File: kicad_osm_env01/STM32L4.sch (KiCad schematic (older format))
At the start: 10 parts

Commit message: kicad review sch initial
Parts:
- added D?: STM_STATUS, symbol device:LED
- added R?: 330R, Resistor_SMD:R_0603_1608Metric, symbol OSM_env01-rescue:R-device-ESP32-EVB_Rev_D-rescue
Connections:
- net GND: now also D?.1 (K)
- net PA15: no longer names the net of U?.25 (PA15)
- net PA15: now also R?.1
- new net: D?.2 (A), R?.2
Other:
- note added: "check led polarity\n"
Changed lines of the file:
@@
 $Descr A4 11693 8268
 encoding utf-8
-Sheet 8 9
+Sheet 5 9
 Title ""
 Date ""
@@
 Wire Wire Line
 	8675 3325 8575 3325
-Text HLabel 8675 3425 2    50   Input ~ 0
-PA15
-Wire Wire Line
-	8675 3425 8575 3425
 Text HLabel 8675 3525 2    50   Input ~ 0
 PA14
@@
 Wire Wire Line
 	8675 3625 8575 3625
+Wire Wire Line
+	10100 3425 10400 3425
+$Comp
+L OSM_env01-rescue:GND-ESP32-EVB_Rev_D #PWR?
+U 1 1 60BF8FB6
+P 10400 3425
+AR Path="/60BF8FB6" Ref="#PWR?"  Part="1"
+AR Path="/60917DD5/60BF8FB6" Ref="#PWR?"  Part="1"
+F 0 "#PWR?" H 10400 3175 50  0001 C CNN
+F 1 "GND" H 10405 3252 50  0000 C CNN
+F 2 "" H 10400 3425 60  0000 C CNN
+F 3 "" H 10400 3425 60  0000 C CNN
+	1    10400 3425
+	1    0    0    -1
+$EndComp
+Wire Wire Line
+	9800 3425 9650 3425
+$Comp
+L OSM_env01-rescue:R-device-ESP32-EVB_Rev_D-rescue R?
+U 1 1 60BF8FBD
+P 9500 3425
+AR Path="/60BF8FBD" Ref="R?"  Part="1"
+AR Path="/60917DD5/60BF8FBD" Ref="R?"  Part="1"
+F 0 "R?" V 9293 3425 50  0000 C CNN
+F 1 "330R" V 9384 3425 50  0000 C CNN
+F 2 "Resistor_SMD:R_0603_1608Metric" V 9430 3425 50  0001 C CNN
+F 3 "" H 9500 3425 50  0001 C CNN
+	1    9500 3425
+	0    -1   -1   0
+$EndComp
+Wire Wire Line
+	8575 3425 9350 3425
+$Comp
+L device:LED D?
+U 1 1 60C00D45
+P 9950 3425
+F 0 "D?" H 9943 3170 50  0000 C CNN
+F 1 "STM_STATUS" H 9943 3261 50  0000 C CNN
+F 2 "" H 9950 3425 50  0001 C CNN
+F 3 "~" H 9950 3425 50  0001 C CNN
+	1    9950 3425
+	-1   0    0    1
+$EndComp
+Text Notes 10100 3925 0    50   ~ 0
+check led polarity\n
 $EndSCHEMATC

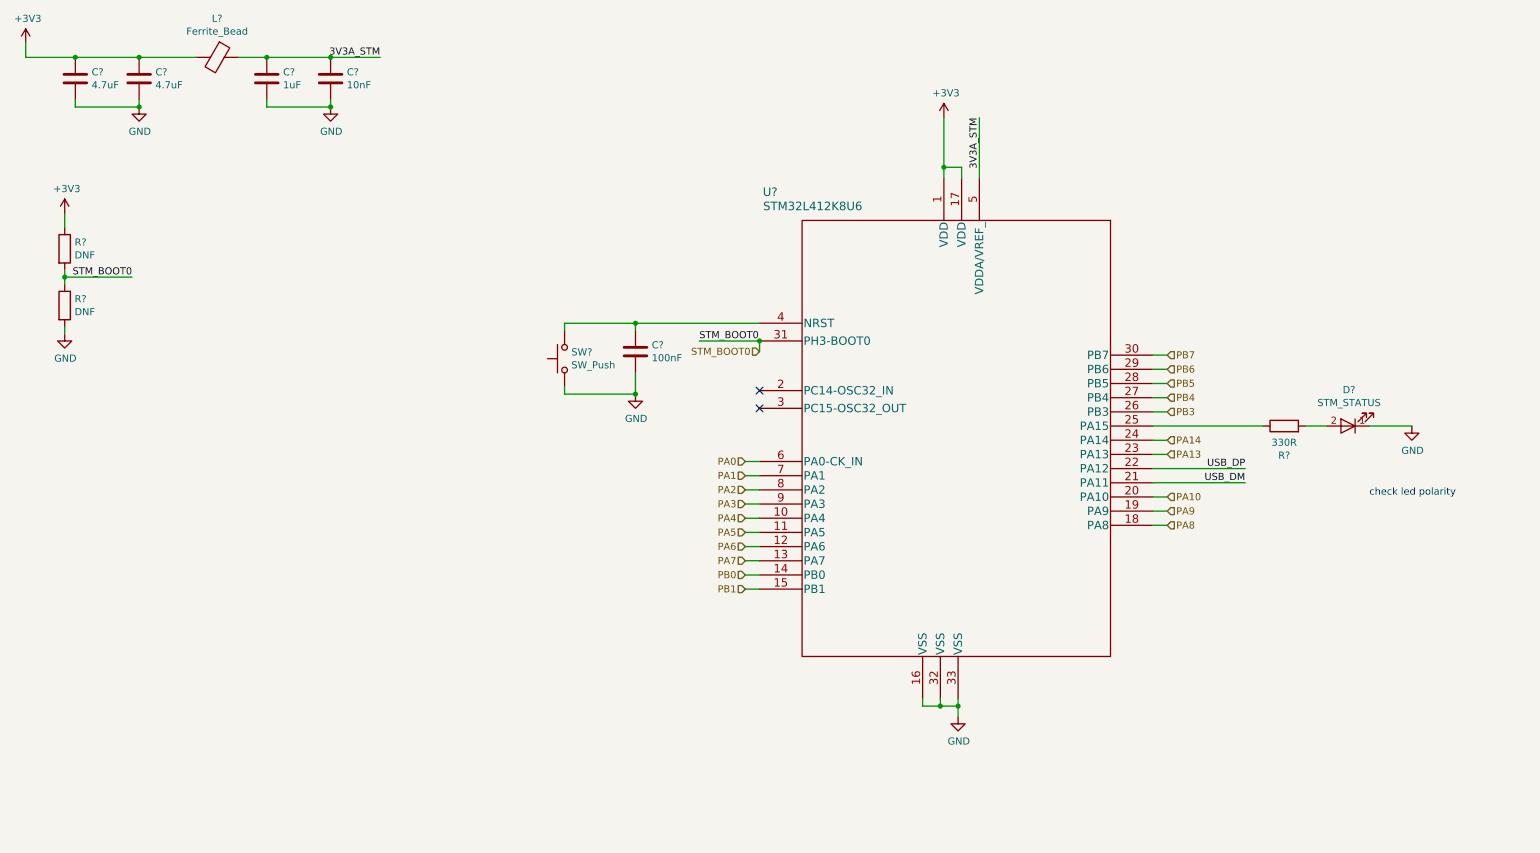
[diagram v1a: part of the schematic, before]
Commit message: updated schematics
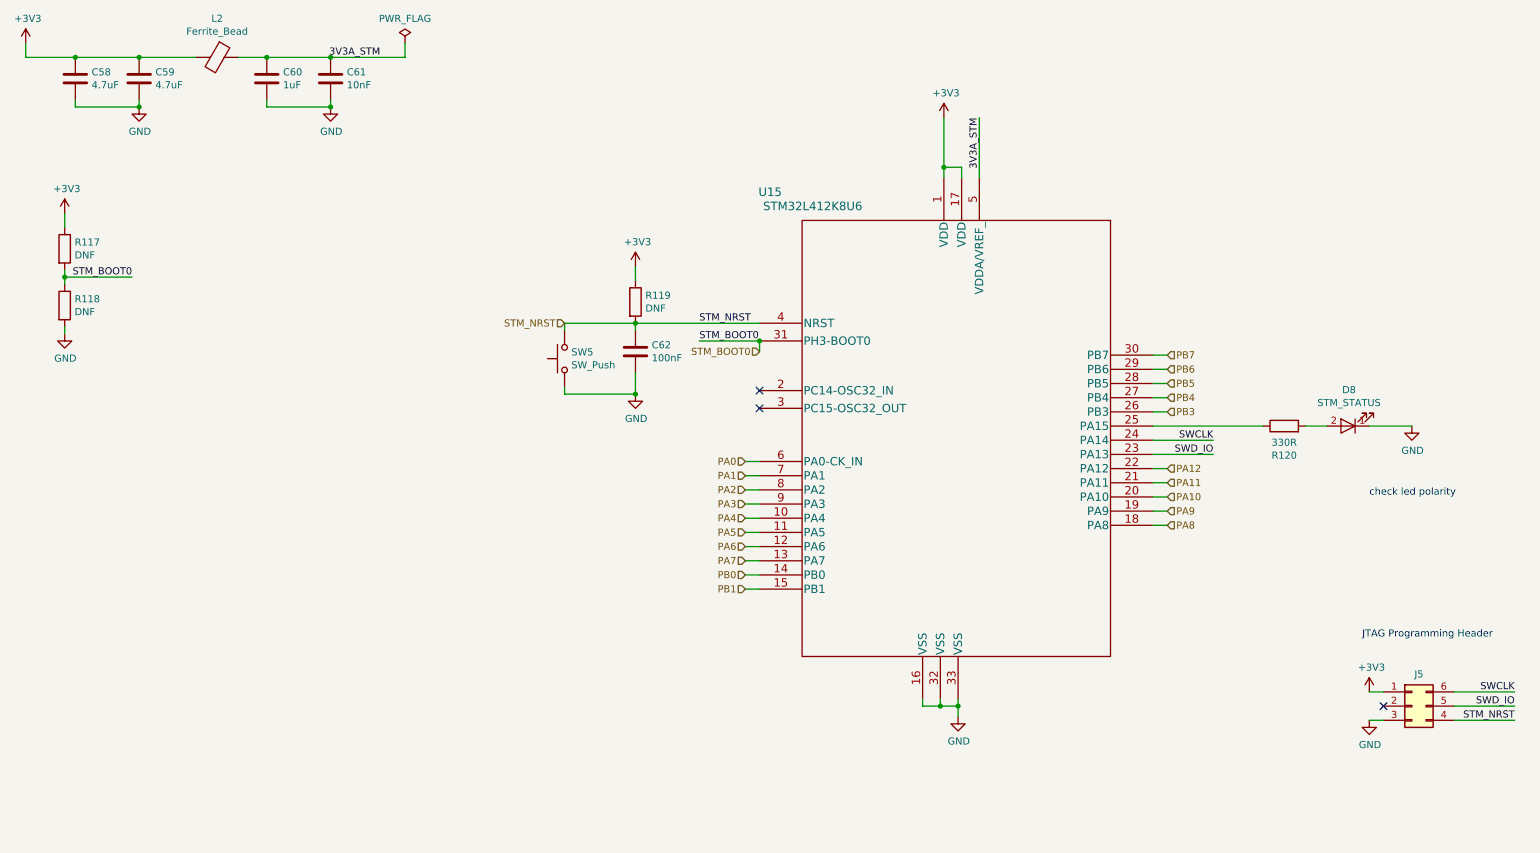
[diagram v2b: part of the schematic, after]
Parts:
- added J5: Conn_02x03_Counter_Clockwise, symbol Connector:Conn_02x03_Counter_Clockwise
- added R119: DNF, symbol device:R
- gave numbers to parts that had none: 12
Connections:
- net +3V3: now also J5.1 (Pin_1), R119.1
- net GND: now also J5.3 (Pin_3)
- net STM_NRST: now reaches C62.1, SW5.2, U15.4 (NRST)
- net STM_NRST: now also J5.4 (Pin_4), R119.2
- net PA13 renamed SWD_IO
- net SWD_IO: now also J5.5 (Pin_5)
- net PA14 renamed SWCLK
- net SWCLK: now also J5.6 (Pin_6)
- net USB_DM renamed PA11
- net USB_DP renamed PA12
- no-connect marks 2 -> 3
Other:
- note added: "JTAG Programming Header"

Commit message: schematics awaiting review
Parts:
- added TP85: Test_Point, TestPoint:TestPoint_THTPad_D1.0mm_Drill0.5mm, symbol OSM_env01-rescue:Test_Point-Connector-ESP32-EVB_Rev_D-rescue
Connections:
- net 3V3A_STM: now also TP85.1
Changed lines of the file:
@@
 Wire Wire Line
 	2775 825  3300 825
+$Comp
+L OSM_env01-rescue:Test_Point-Connector-ESP32-EVB_Rev_D-rescue TP?
+U 1 1 60C1B460
+P 3300 825
+AR Path="/60C1B460" Ref="TP?"  Part="1"
+AR Path="/608F4675/60C1B460" Ref="TP?"  Part="1"
+AR Path="/60917DD5/60C1B460" Ref="TP85"  Part="1"
+F 0 "TP85" V 3300 1075 50  0000 C CNN
+F 1 "Test_Point" V 3300 1200 50  0001 C CNN
+F 2 "TestPoint:TestPoint_THTPad_D1.0mm_Drill0.5mm" H 3500 825 50  0001 C CNN
+F 3 "~" H 3500 825 50  0001 C CNN
+	1    3300 825
+	0    1    -1   0
+$EndComp
 $EndSCHEMATC

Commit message: updated schematics
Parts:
- C58, C59, C60, C61, C62: footprint (none) -> Capacitor_SMD:C_0603_1608Metric
- D8: footprint (none) -> LED_SMD:LED_0603_1608Metric
- J5: footprint (none) -> Connector_PinHeader_2.54mm:PinHeader_2x03_P2.54mm_Vertical
- L2: footprint (none) -> Inductor_SMD:L_0805_2012Metric
- R117, R118, R119: footprint (none) -> Resistor_SMD:R_0603_1608Metric
- SW5: footprint (none) -> Button_Switch_SMD:SW_SPST_B3U-1000P
- U15: footprint QFN32_5X5_STM -> Package_DFN_QFN:QFN-32-1EP_5x5mm_P0.5mm_EP3.1x3.1mm
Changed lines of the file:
@@
 $Descr A4 11693 8268
 encoding utf-8
-Sheet 10 11
+Sheet 10 12
 Title ""
 Date ""
@@
 F 0 "C58" H 1090 1021 50  0000 L CNN
 F 1 "4.7uF" H 1090 930 50  0000 L CNN
-F 2 "" H 1013 825 50  0001 C CNN
+F 2 "Capacitor_SMD:C_0603_1608Metric" H 1013 825 50  0001 C CNN
 F 3 "" H 975 975 50  0001 C CNN
 	1    975  975
@@
 F 0 "C59" H 1540 1021 50  0000 L CNN
 F 1 "4.7uF" H 1540 930 50  0000 L CNN
-F 2 "" H 1463 825 50  0001 C CNN
+F 2 "Capacitor_SMD:C_0603_1608Metric" H 1463 825 50  0001 C CNN
 F 3 "" H 1425 975 50  0001 C CNN
 	1    1425 975
@@
 F 0 "C60" H 2440 1021 50  0000 L CNN
 F 1 "1uF" H 2440 930 50  0000 L CNN
-F 2 "" H 2363 825 50  0001 C CNN
+F 2 "Capacitor_SMD:C_0603_1608Metric" H 2363 825 50  0001 C CNN
 F 3 "" H 2325 975 50  0001 C CNN
 	1    2325 975
@@
 F 0 "C61" H 2890 1021 50  0000 L CNN
 F 1 "10nF" H 2890 930 50  0000 L CNN
-F 2 "" H 2813 825 50  0001 C CNN
+F 2 "Capacitor_SMD:C_0603_1608Metric" H 2813 825 50  0001 C CNN
 F 3 "" H 2775 975 50  0001 C CNN
 	1    2775 975
@@
 F 0 "L2" V 1701 825 50  0000 C CNN
 F 1 "Ferrite_Bead" V 1792 825 50  0000 C CNN
-F 2 "" V 1905 825 50  0001 C CNN
+F 2 "Inductor_SMD:L_0805_2012Metric" V 1905 825 50  0001 C CNN
 F 3 "" H 1975 825 50  0001 C CNN
 	1    1975 825
@@
 F 0 "U15" H 5875 2575 60  0000 C CNN
 F 1 "STM32L412K8U6" H 6175 2475 60  0000 C CNN
-F 2 "QFN32_5X5_STM" H 7200 2415 60  0001 C CNN
+F 2 "Package_DFN_QFN:QFN-32-1EP_5x5mm_P0.5mm_EP3.1x3.1mm" H 7200 2415 60  0001 C CNN
 F 3 "" H 5800 2175 60  0000 C CNN
 	1    5800 2175
@@
 F 0 "R118" H 970 2621 50  0000 L CNN
 F 1 "DNF" H 970 2530 50  0000 L CNN
-F 2 "" V 830 2575 50  0001 C CNN
+F 2 "Resistor_SMD:R_0603_1608Metric" V 830 2575 50  0001 C CNN
 F 3 "" H 900 2575 50  0001 C CNN
 	1    900  2575
@@
 F 0 "R117" H 970 2221 50  0000 L CNN
 F 1 "DNF" H 970 2130 50  0000 L CNN
-F 2 "" V 830 2175 50  0001 C CNN
+F 2 "Resistor_SMD:R_0603_1608Metric" V 830 2175 50  0001 C CNN
 F 3 "" H 900 2175 50  0001 C CNN
 	1    900  2175
@@
 F 0 "C62" H 5040 2946 50  0000 L CNN
 F 1 "100nF" H 5040 2855 50  0000 L CNN
-F 2 "" H 4963 2750 50  0001 C CNN
+F 2 "Capacitor_SMD:C_0603_1608Metric" H 4963 2750 50  0001 C CNN
 F 3 "" H 4925 2900 50  0001 C CNN
 	1    4925 2900
@@
 F 0 "SW5" V 4471 2902 50  0000 R CNN
 F 1 "SW_Push" V 4380 2902 50  0000 R CNN
-F 2 "" H 4425 3150 50  0001 C CNN
+F 2 "Button_Switch_SMD:SW_SPST_B3U-1000P" H 4425 3150 50  0001 C CNN
 F 3 "" H 4425 3150 50  0001 C CNN
 	1    4425 2950
@@
 F 0 "D8" H 9943 3170 50  0000 C CNN
 F 1 "STM_STATUS" H 9943 3261 50  0000 C CNN
-F 2 "" H 9950 3425 50  0001 C CNN
+F 2 "LED_SMD:LED_0603_1608Metric" H 9950 3425 50  0001 C CNN
 F 3 "~" H 9950 3425 50  0001 C CNN
 	1    9950 3425
@@
 F 0 "R119" H 4995 2596 50  0000 L CNN
 F 1 "DNF" H 4995 2505 50  0000 L CNN
-F 2 "" V 4855 2550 50  0001 C CNN
+F 2 "Resistor_SMD:R_0603_1608Metric" V 4855 2550 50  0001 C CNN
 F 3 "" H 4925 2550 50  0001 C CNN
 	1    4925 2550
@@
 F 0 "J5" H 10450 5625 50  0000 C CNN
 F 1 "Conn_02x03_Counter_Clockwise" H 10450 5626 50  0001 C CNN
-F 2 "" H 10400 5400 50  0001 C CNN
+F 2 "Connector_PinHeader_2.54mm:PinHeader_2x03_P2.54mm_Vertical" H 10400 5400 50  0001 C CNN
 F 3 "~" H 10400 5400 50  0001 C CNN
 	1    10400 5400

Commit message: Throwdown of parts
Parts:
- removed R117, R118: DNF, Resistor_SMD:R_0603_1608Metric, symbol device:R
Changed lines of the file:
@@
 	5800 2825 5375 2825
-Wire Wire Line
-	900  2375 1375 2375
-Text Label 1375 2375 2    50   ~ 0
-STM_BOOT0
-Wire Wire Line
-	900  2375 900  2325
-Connection ~ 900  2375
-$Comp
-L power:+3V3 #PWR?
-U 1 1 60931F89
-P 900 1925
-AR Path="/60931F89" Ref="#PWR?"  Part="1"
-AR Path="/60917DD5/60931F89" Ref="#PWR0112"  Part="1"
-F 0 "#PWR0112" H 900 1775 50  0001 C CNN
-F 1 "+3V3" H 915 2098 50  0000 C CNN
-F 2 "" H 900 1925 50  0001 C CNN
-F 3 "" H 900 1925 50  0001 C CNN
-	1    900  1925
-	1    0    0    -1
-$EndComp
-Wire Wire Line
-	900  2025 900  1925
-Wire Wire Line
-	900  2775 900  2725
-$Comp
-L power:GND #PWR?
-U 1 1 60931F91
-P 900 2775
-AR Path="/60931F91" Ref="#PWR?"  Part="1"
-AR Path="/60917DD5/60931F91" Ref="#PWR0113"  Part="1"
-F 0 "#PWR0113" H 900 2525 50  0001 C CNN
-F 1 "GND" H 905 2602 50  0000 C CNN
-F 2 "" H 900 2775 50  0001 C CNN
-F 3 "" H 900 2775 50  0001 C CNN
-	1    900  2775
-	1    0    0    -1
-$EndComp
-Wire Wire Line
-	900  2425 900  2375
-$Comp
-L device:R R?
-U 1 1 60931F98
-P 900 2575
-AR Path="/60931F98" Ref="R?"  Part="1"
-AR Path="/60917DD5/60931F98" Ref="R118"  Part="1"
-F 0 "R118" H 970 2621 50  0000 L CNN
-F 1 "DNF" H 970 2530 50  0000 L CNN
-F 2 "Resistor_SMD:R_0603_1608Metric" V 830 2575 50  0001 C CNN
-F 3 "" H 900 2575 50  0001 C CNN
-	1    900  2575
-	1    0    0    -1
-$EndComp
-$Comp
-L device:R R?
-U 1 1 60931F9E
-P 900 2175
-AR Path="/60931F9E" Ref="R?"  Part="1"
-AR Path="/60917DD5/60931F9E" Ref="R117"  Part="1"
-F 0 "R117" H 970 2221 50  0000 L CNN
-F 1 "DNF" H 970 2130 50  0000 L CNN
-F 2 "Resistor_SMD:R_0603_1608Metric" V 830 2175 50  0001 C CNN
-F 3 "" H 900 2175 50  0001 C CNN
-	1    900  2175
-	1    0    0    -1
-$EndComp
 Wire Wire Line
 	4925 2700 5800 2700

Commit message: updated 3d step file
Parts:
- U15: symbol Devtank:STM32L412K8U6 -> OSM_env01-rescue:STM32L412K8U6-Devtank
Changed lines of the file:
@@
 STM_BOOT0
 $Comp
-L Devtank:STM32L412K8U6 U?
+L OSM_env01-rescue:STM32L412K8U6-Devtank U?
 U 1 1 60931F7E
 P 5800 2175

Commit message: added stm to schematic
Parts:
- removed D8: STM_STATUS, LED_SMD:LED_0603_1608Metric, symbol device:LED
- removed R120: 330R, Resistor_SMD:R_0603_1608Metric, symbol OSM_env01-rescue:R-device-ESP32-EVB_Rev_D-rescue
- removed U15: STM32L412K8U6, Package_DFN_QFN:QFN-32-1EP_5x5mm_P0.5mm_EP3.1x3.1mm, symbol OSM_env01-rescue:STM32L412K8U6-Devtank
- added C? (x2): 18pF, symbol device:C
- added C? (x2): 4.3pF, symbol device:C
- added D?: GRN, symbol device:LED
- added R? (x2): R, symbol device:R
- added R?: 330R, symbol device:R
- added U?: STM32L451RCTx, LQFP64, symbol Devtank:STM32L451RCTx
- added Y?: 8MHZ, symbol device:Crystal_GND24
- added Y?: ABS25-32.768KHZ-6-T, symbol device:Crystal_GND23
- L2: value Ferrite_Bead -> 2A/0.05DCR
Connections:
- net +3V3: now also D?.2 (A), R?.1, U?.19 (VDD), U?.32 (VDD), U?.48 (VDD), U?.64 (VDD)
- net 3V3A_STM: now also U?.13 (VDDA)
- net GND: now also C?.1, C?.1, C?.1, C?.1, R?.1, U?.12 (VSSA), U?.18 (VSS), U?.31 (VSS), U?.47 (VSS), U?.63 (VSS), Y?.2, Y?.2, Y?.3, Y?.4
- net STM_BOOT0: now also R?.2, R?.2, U?.60 (BOOT0)
- net STM_NRST: now also U?.7 (NRST)
- net SWCLK: now also U?.49 (SYS_JTCK-SWCLK/PA14)
- net SWD_IO: now also U?.46 (IR_OUT/SYS_JTMS-SWDIO/USB_OTG_FS_NOE/PA13)
- new net: D?.1 (K), R?.2
- new net 32.768KHZ_crystal_in: C?.2, U?.3 (PC14/RCC_OSC32_IN), Y?.1
- new net 32.768KHZ_crystal_out: C?.2, U?.4 (PC15/ADC1_EXTI15/ADC2_EXTI15/ADC3_EXTI15/RCC_OSC32_OUT), Y?.4
- new net 8MHZ_crystal_in: C?.2, U?.5 (PH0/RCC_OSC_IN), Y?.1
- new net 8MHZ_crystal_out: C?.2, U?.6 (PH1/RCC_OSC_OUT), Y?.3
- new net ADC1: U?.8 (PC0/ADC1_IN1/ADC2_IN1/ADC3_IN1/DFSDM_DATIN4/I2C3_SCL/LCD_SEG18/LPTIM1_IN1/LPTIM2_IN1/LPUART1_RX)
- new net ADC2: U?.9 (PC1/ADC1_IN2/ADC2_IN2/ADC3_IN2/DFSDM_CKIN4/I2C3_SDA/LCD_SEG19/LPTIM1_OUT/LPUART1_TX)
- new net ADC3: U?.10 (PC2/ADC1_IN3/ADC2_IN3/ADC3_IN3/DFSDM_CKOUT/LCD_SEG20/LPTIM1_IN2/SPI2_MISO)
- new net ADC4: U?.11 (PC3/ADC1_IN4/ADC2_IN4/ADC3_IN4/LCD_VLCD/LPTIM1_ETR/LPTIM2_ETR/SAI1_SD_A/SPI2_MOSI)
- new net ADC5: U?.14 (ADC1_IN5/ADC2_IN5/OPAMP1_VINP/RTC_TAMP2/SAI1_EXTCLK/SYS_WKUP1/TIM2_CH1/TIM2_ETR/TIM5_CH1/TIM8_ETR/UART4_TX/USART2_CTS/PA0)
- new net ADC6: U?.15 (ADC1_IN6/ADC2_IN6/LCD_SEG0/OPAMP1_VINM/TIM15_CH1N/TIM2_CH2/TIM5_CH2/UART4_RX/USART2_DE/USART2_RTS/PA1)
- new net CAN1_RX: U?.33 (DFSDM_DATIN1/I2C2_SMBA/LCD_SEG12/LPUART1_DE/LPUART1_RTS/SAI2_FS_A/SPI2_NSS/SWPMI1_IO/TIM15_BKIN/TIM1_BKIN/TIM1_BKIN_COMP2/TSC_G1_IO1/USART3_CK/PB12)
- new net CAN1_TX: U?.34 (DFSDM_CKIN1/I2C2_SCL/LCD_SEG13/LPUART1_CTS/SAI2_SCK_A/SPI2_SCK/SWPMI1_TX/TIM15_CH1N/TIM1_CH1N/TSC_G1_IO2/USART3_CTS/PB13)
- new net GPIO1: U?.37 (PC6/DFSDM_CKIN3/LCD_SEG24/SAI2_MCLK_A/SDMMC1_D6/TIM3_CH1/TIM8_CH1/TSC_G4_IO1)
- new net GPIO2: U?.38 (PC7/DFSDM_DATIN3/LCD_SEG25/SAI2_MCLK_B/SDMMC1_D7/TIM3_CH2/TIM8_CH2/TSC_G4_IO2)
- new net GPIO3: U?.39 (PC8/LCD_SEG26/SDMMC1_D0/TIM3_CH3/TIM8_CH3/TSC_G4_IO3)
- new net GPIO4: U?.40 (PC9/DAC1_EXTI9/LCD_SEG27/SAI2_EXTCLK/SDMMC1_D1/TIM3_CH4/TIM8_BKIN2/TIM8_BKIN2_COMP1/TIM8_CH4/TSC_G4_IO4/USB_OTG_FS_NOE)
- new net GPIO5: U?.51 (PC10/LCD_COM4/LCD_SEG28/LCD_SEG40/SAI2_SCK_B/SDMMC1_D2/SPI3_SCK/TSC_G3_IO2/UART4_TX/USART3_TX)
- new net GPIO6: U?.52 (PC11/ADC1_EXTI11/ADC2_EXTI11/ADC3_EXTI11/LCD_COM5/LCD_SEG29/LCD_SEG41/SAI2_MCLK_B/SDMMC1_D3/SPI3_MISO/TSC_G3_IO3/UART4_RX/USART3_RX)
- new net I2C1_SCL: U?.42 (DAC1_EXTI9/LCD_COM1/TIM15_BKIN/TIM1_CH2/USART1_TX/USB_OTG_FS_VBUS/PA9)
- new net I2C1_SDA: U?.43 (LCD_COM2/TIM17_BKIN/TIM1_CH3/USART1_RX/USB_OTG_FS_ID/PA10)
- new net LPUART1_RX: U?.29 (COMP1_OUT/DFSDM_DATIN7/I2C2_SCL/LCD_SEG10/LPUART1_RX/QUADSPI_CLK/SAI1_SCK_A/SPI2_SCK/TIM2_CH3/USART3_TX/PB10)
- new net LPUART1_TX: U?.30 (ADC1_EXTI11/ADC2_EXTI11/ADC3_EXTI11/COMP2_OUT/DFSDM_CKIN7/I2C2_SDA/LCD_SEG11/LPUART1_TX/QUADSPI_NCS/TIM2_CH4/USART3_RX/PB11)
- new net SPI1_CS: U?.20 (ADC1_IN9/ADC2_IN9/DAC1_OUT1/LPTIM2_OUT/SAI1_FS_B/SPI1_NSS/SPI3_NSS/USART2_CK/PA4)
- new net SPI1_MISO: U?.22 (ADC1_IN11/ADC2_IN11/LCD_SEG3/OPAMP2_VINP/QUADSPI_BK1_IO3/SPI1_MISO/TIM16_CH1/TIM1_BKIN/TIM1_BKIN_COMP2/TIM3_CH1/TIM8_BKIN/TIM8_BKIN_COMP2/USART3_CTS/PA6)
- new net SPI1_MOSI: U?.23 (ADC1_IN12/ADC2_IN12/LCD_SEG4/OPAMP2_VINM/QUADSPI_BK1_IO2/SPI1_MOSI/TIM17_CH1/TIM1_CH1N/TIM3_CH2/TIM8_CH1N/PA7)
- new net SPI1_SCK: U?.21 (ADC1_IN10/ADC2_IN10/DAC1_OUT2/LPTIM2_ETR/SPI1_SCK/TIM2_CH1/TIM2_ETR/TIM8_CH1N/PA5)
- new net USART1_RX: U?.59 (COMP2_INM/DFSDM_CKIN5/I2C1_SDA/LCD_SEG21/LPTIM1_IN2/SYS_PVD_IN/TIM17_CH1N/TIM4_CH2/TIM8_BKIN/TIM8_BKIN_COMP1/TSC_G2_IO4/UART4_CTS/USART1_RX/PB7)
- new net USART1_TX: U?.58 (COMP2_INP/DFSDM_DATIN5/I2C1_SCL/LPTIM1_ETR/SAI1_FS_B/TIM16_CH1N/TIM4_CH1/TIM8_BKIN2/TIM8_BKIN2_COMP2/TSC_G2_IO3/USART1_TX/PB6)
- new net USART2_RX: U?.17 (ADC1_IN8/ADC2_IN8/LCD_SEG2/OPAMP1_VOUT/TIM15_CH2/TIM2_CH4/TIM5_CH4/USART2_RX/PA3)
- new net USART2_TX: U?.16 (ADC1_IN7/ADC2_IN7/LCD_SEG1/RCC_LSCO/SAI2_EXTCLK/SYS_WKUP4/TIM15_CH1/TIM2_CH3/TIM5_CH3/USART2_TX/PA2)
- new net USART3_RX: U?.25 (PC5/ADC1_IN14/ADC2_IN14/COMP1_INP/LCD_SEG23/SYS_WKUP5/USART3_RX)
- new net USART3_TX: U?.24 (PC4/ADC1_IN13/ADC2_IN13/COMP1_INM/LCD_SEG22/USART3_TX)
- new net status_led: R?.1, U?.26 (ADC1_IN15/ADC2_IN15/COMP1_OUT/LCD_SEG5/OPAMP2_VOUT/QUADSPI_BK1_IO1/TIM1_CH2N/TIM3_CH3/TIM8_CH2N/USART3_CK/PB0)
- no-connect marks 3 -> 1
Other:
- note added: "Note: For comfirmation of pin functions refer to datasheet. Symbol may not be correct\n"
- note added: "make sure LED polarity is correct"
- note removed: "Fast adc channels are PC0-PC3, PA0 and PA1 the rest are slow"
- note removed: "I/O with wakeup from standby/shutdown capability are PA0, PC13, PA2, PC5\n"
- note removed: "check led polarity\n"
- moved on the sheet: C62, J5, R119, SW5
